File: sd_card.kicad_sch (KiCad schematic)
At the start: 2 parts, among them J4 Micro_SD_Card

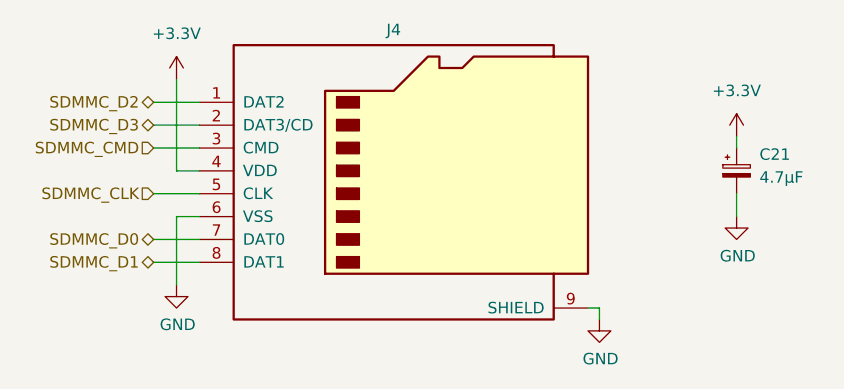
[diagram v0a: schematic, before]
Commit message: Route PCB tracks
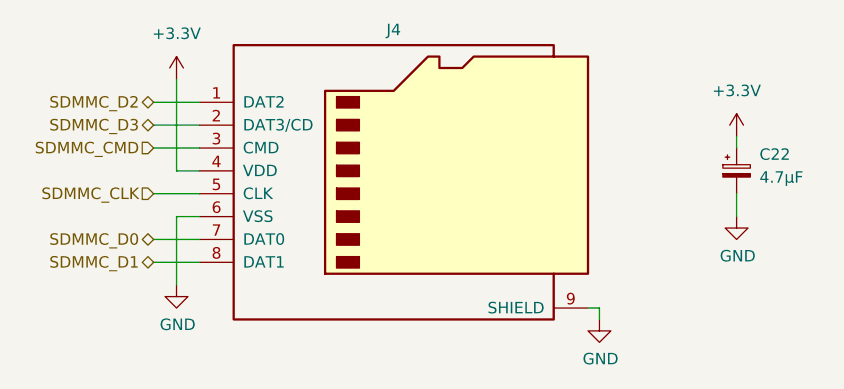
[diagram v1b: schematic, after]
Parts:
- renumbered C21 to C22
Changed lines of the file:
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@@
   (title_block
     (title "SD Card")
-    (date "2022-12-23")
+    (date "2023-01-17")
     (rev "${REVISION}")
     (company "Authors: H. Fedarovich, I. Kajdan")
@@
   (symbol (lib_id "Device:C_Polarized_Small") (at 190.5 100.33 0) (unit 1)
     (in_bom yes) (on_board yes) (fields_autoplaced)
-    (property "Reference" "C21" (id 0) (at 193.04 98.5138 0)
+    (property "Reference" "C22" (id 0) (at 193.04 98.5138 0)
       (effects (font (size 1.27 1.27)) (justify left))
     )
@@
   (symbol (lib_id "power:GND") (at 190.5 105.41 0) (unit 1)
     (in_bom yes) (on_board yes)
-    (property "Reference" "#PWR051" (id 0) (at 190.5 111.76 0)
+    (property "Reference" "#PWR052" (id 0) (at 190.5 111.76 0)
       (effects (font (size 1.27 1.27)) hide)
     )
@@
   (symbol (lib_id "power:+3.3V") (at 190.5 96.52 0) (unit 1)
     (in_bom yes) (on_board yes) (fields_autoplaced)
-    (property "Reference" "#PWR050" (id 0) (at 190.5 100.33 0)
+    (property "Reference" "#PWR051" (id 0) (at 190.5 100.33 0)
       (effects (font (size 1.27 1.27)) hide)
     )
@@
   (symbol (lib_id "power:+3.3V") (at 128.27 90.17 0) (unit 1)
     (in_bom yes) (on_board yes) (fields_autoplaced)
-    (property "Reference" "#PWR049" (id 0) (at 128.27 93.98 0)
+    (property "Reference" "#PWR050" (id 0) (at 128.27 93.98 0)
       (effects (font (size 1.27 1.27)) hide)
     )
@@
   (symbol (lib_id "power:GND") (at 128.27 113.03 0) (unit 1)
     (in_bom yes) (on_board yes)
-    (property "Reference" "#PWR052" (id 0) (at 128.27 119.38 0)
+    (property "Reference" "#PWR053" (id 0) (at 128.27 119.38 0)
       (effects (font (size 1.27 1.27)) hide)
     )
@@
   (symbol (lib_id "power:GND") (at 175.26 116.84 0) (unit 1)
     (in_bom yes) (on_board yes)
-    (property "Reference" "#PWR053" (id 0) (at 175.26 123.19 0)
+    (property "Reference" "#PWR054" (id 0) (at 175.26 123.19 0)
       (effects (font (size 1.27 1.27)) hide)
     )
